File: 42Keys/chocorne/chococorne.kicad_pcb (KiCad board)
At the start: 2 copper layers, 129.4 x 90.4 mm, 54 parts, among them J1 MJ-4PP-9, J2 OLED, SW1 SW_PUSH, SW10 SW_PUSH, SW11 SW_PUSH, SW12 SW_PUSH, SW13 SW_PUSH, SW14 SW_PUSH, SW15 SW_PUSH, SW16 SW_PUSH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

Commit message: But, is it a corne?
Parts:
- moved SW19 1.75 mm to (133.3, 113.8)
- moved SW20 1.75 mm to (153.3, 116.4)
- moved SW21 1.75 mm to (174.6, 119.7)
- moved D21 0.53 mm to (167.4, 92.7)
- moved J2 0.50 mm to (173.7, 90.5)
- moved JP61 0.50 mm to (173.7, 87.9)
- moved JP63 0.50 mm to (176.2, 87.8)
- moved JP64 0.50 mm to (176.2, 87.8)
- moved JP65 0.50 mm to (178.8, 87.8)
- moved JP66 0.50 mm to (178.8, 87.8)
- moved JP68 0.50 mm to (181.4, 87.8)
- moved JP6 0.50 mm to (181.4, 87.8)
- moved JP62 0.50 mm to (173.7, 87.9)
- moved U1 0.44 mm to (178.4, 71.4)
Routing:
- net row0: track 130.1 -> 157.8 mm, vias 1 -> 0
- net Net-(U1-Pad13): track 23.3 -> 38.5 mm, vias 1 -> 0
- net reset: track 59.6 -> 67.3 mm
- net data: track 69.6 -> 77.2 mm
- net Net-(U1-Pad11): track 33.2 -> 26.2 mm
- net SDA: track 64.5 -> 70.5 mm, vias 2 -> 1
- net GND: track 93.8 -> 88.4 mm, vias 0 -> 1
- net Net-(U1-Pad24): track 46.0 -> 50.5 mm
- net Net-(U1-Pad14): track 29.9 -> 26.1 mm
- net VCC: track 61.6 -> 57.8 mm, vias 0 -> 1
- net col1: track 188.0 -> 191.5 mm
- net Net-(D19-Pad2): track 30.6 -> 27.4 mm
- net Net-(D21-Pad2): track 33.4 -> 31.2 mm
- net LED: track 17.1 -> 18.9 mm
- net col5: track 84.2 -> 82.6 mm, vias 1 -> 0
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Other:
- board size 129.4 x 90.4 mm -> 130 x 88.6 mm

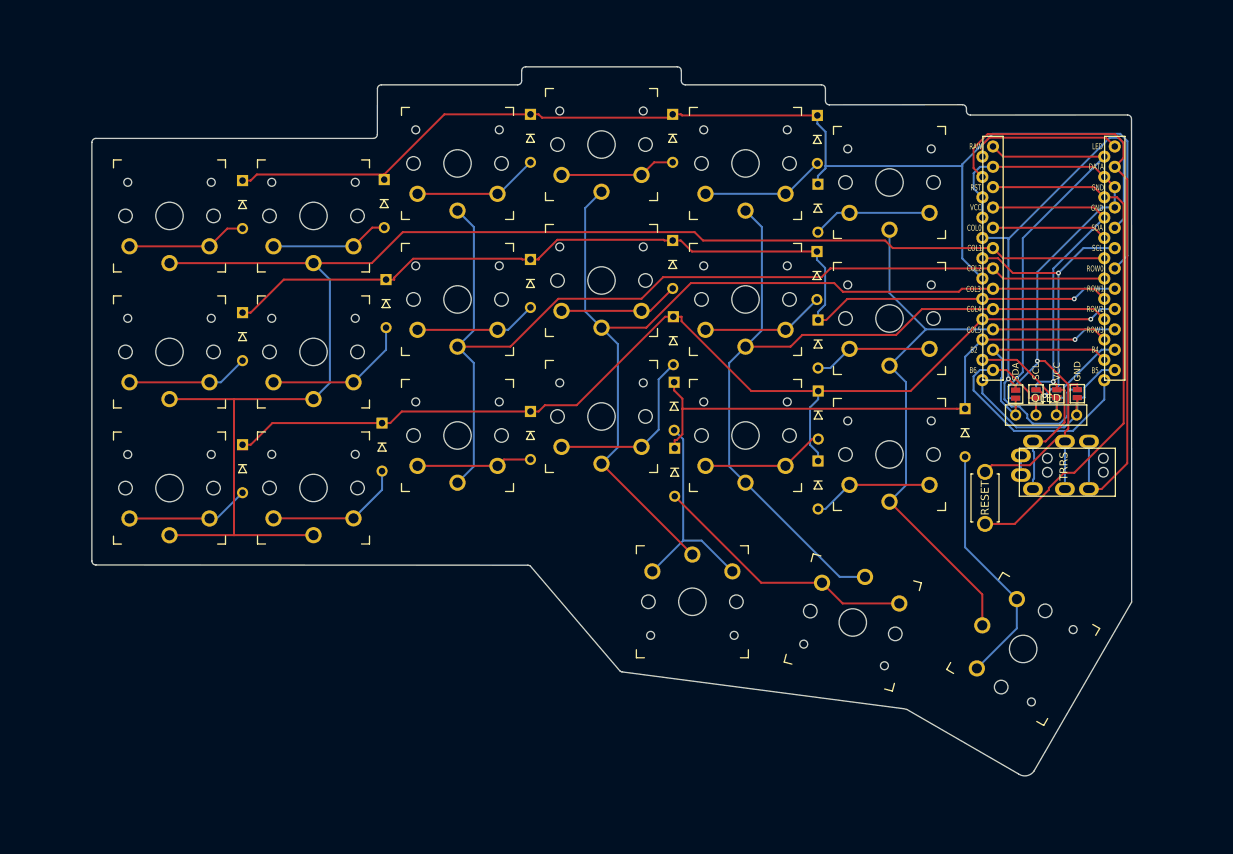
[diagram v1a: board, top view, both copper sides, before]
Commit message: Add back break off, 'fix' 1.5u footprint (maybe) move bits around.
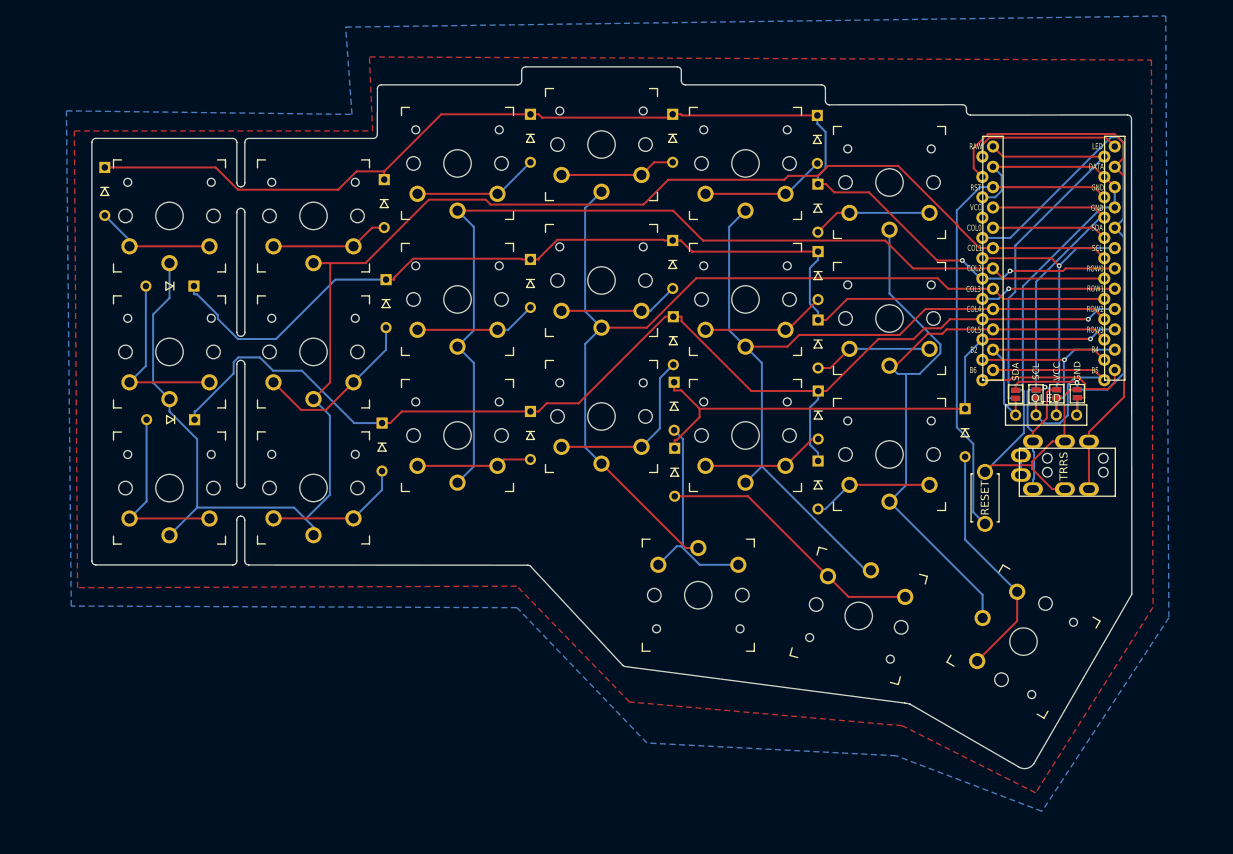
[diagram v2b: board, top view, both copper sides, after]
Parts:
- moved D1 17.3 mm to (59.8, 62.5)
- moved D7 11.1 mm to (68.0, 74.3), turned to 180 degrees
- moved D13 10.9 mm to (68.0, 91.0), turned to 180 degrees
- moved SW20 1.10 mm to (154.1, 115.6)
- moved SW19 1.10 mm to (134.0, 113.0)
- moved SW21 0.92 mm to (174.7, 118.8)
- moved D11 0.14 mm to (149.0, 73.0)
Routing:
- net row2: track 133.7 -> 146.6 mm
- net row1: track 124.5 -> 135.8 mm
- net row0: track 157.8 -> 148.0 mm, vias 0 -> 2
- net col5: track 82.6 -> 91.4 mm
- net col1: track 191.5 -> 199.3 mm
- net Net-(D13-Pad2): track 15.5 -> 23.2 mm
- net Net-(D7-Pad2): track 15.3 -> 22.9 mm
- net data: track 77.2 -> 70.0 mm
- net reset: track 67.3 -> 60.8 mm
- net Net-(U1-Pad13): track 38.5 -> 32.4 mm
- net GND: track 88.4 -> 94.4 mm, vias 1 -> 0
- net VCC: track 57.8 -> 61.8 mm, vias 1 -> 0
- net Net-(D8-Pad2): track 18.5 -> 21.4 mm
- net SDA: track 70.5 -> 68.9 mm
- net Net-(U1-Pad12): track 27.1 -> 26.0 mm
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- added copper zone on B.Cu, net (none)
- added copper zone on F.Cu, net (none)
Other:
- board size 130 x 88.6 mm -> 130 x 87.7 mm

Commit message: tweaks
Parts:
- added H1: h1, kbd:LEGO_HOLE, F.Cu at (185.7, 106.1)
- added h2: h2, kbd:LEGO_HOLE, F.Cu at (171.2, 97.6)
- D1, D10, D11, D12, D13, D14, D15, D16, D17, D18, D19, D2, D20, D21, D3, D4, D5, D6, D7, D8, D9: footprint kbd:D3_TH -> kbd:D3_TH_SMD
- moved RSW1 19.0 mm to (186.0, 90.9)
- moved D21 18.8 mm to (149.1, 97.1)
- moved D18 12.0 mm to (149.1, 87.2)
- moved D19 9.62 mm to (139.3, 84.5), turned to 0 degrees
- moved D17 9.17 mm to (157.4, 86.9), turned to 0 degrees
- moved D11 8.68 mm to (157.1, 69.9), turned to 0 degrees
- moved D12 4.92 mm to (148.9, 76.7)
- moved D20 3.55 mm to (130.9, 94.1)
- moved D10 3.29 mm to (130.9, 68.4)
- moved J1 3.13 mm to (188.0, 100.2)
- moved D6 1.78 mm to (148.9, 66.4)
- moved J2 1.06 mm to (173.9, 89.4)
- moved JP6 1.06 mm to (181.6, 86.8)
- moved JP61 1.06 mm to (173.9, 86.8)
- moved JP62 1.06 mm to (173.9, 86.8)
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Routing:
- net row0: track 148.0 -> 168.3 mm, vias 2 -> 0
- net SDA: track 68.9 -> 49.9 mm, vias 1 -> 2
- net row1: track 135.8 -> 153.9 mm, vias 1 -> 0
- net Net-(D17-Pad2): track 15.5 -> 33.0 mm
- net Net-(D11-Pad2): track 15.6 -> 32.6 mm
- net Net-(D19-Pad2): track 27.0 -> 40.5 mm
- net reset: track 60.8 -> 48.4 mm
- net row2: track 146.6 -> 158.5 mm
- net Net-(D21-Pad2): track 30.3 -> 42.1 mm
- net GND: track 94.4 -> 83.3 mm, vias 0 -> 1
- net Net-(U1-Pad13): track 32.4 -> 23.5 mm
- net Net-(D18-Pad2): track 15.2 -> 23.8 mm
- net VCC: track 61.8 -> 69.9 mm, vias 0 -> 2
- net row3: track 71.3 -> 78.8 mm
- net Net-(D10-Pad2): track 15.1 -> 21.0 mm
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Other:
- outline, holes or cut-outs redrawn

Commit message: fix screens?
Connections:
- U1 pad 11: Net-(U1-Pad11) -> (no net)
- U1 pad 12: Net-(U1-Pad12) -> (no net)
- U1 pad 13: Net-(U1-Pad13) -> (no net)
- U1 pad 14: Net-(U1-Pad14) -> (no net)
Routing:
- net Net-(U1-Pad14): track 25.4 -> 2.11 mm
- net Net-(U1-Pad11): track 27.3 -> 4.36 mm, vias 1 -> 0
- net Net-(U1-Pad12): track 26.0 -> 4.42 mm
- net col5: track 89.0 -> 109.7 mm
- net Net-(U1-Pad13): track 23.5 -> 4.27 mm
- net data: track 72.0 -> 62.0 mm
- net col3: track 121.7 -> 129.3 mm, vias 1 -> 0
- net Net-(U1-Pad24): track 46.0 -> 52.7 mm
- net VCC: track 69.9 -> 76.5 mm, vias 2 -> 1
- net GND: track 83.3 -> 89.8 mm, vias 1 -> 0
- net col2: track 125.1 -> 129.0 mm, vias 1 -> 0
- net col1: track 196.7 -> 199.3 mm
- net Net-(D21-Pad2): track 42.1 -> 44.4 mm
- net SDA: track 49.9 -> 52.2 mm, vias 2 -> 1
- net col4: track 105.3 -> 107.3 mm
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
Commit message: really fix screen, try not to route vcc to gnd...
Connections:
- JP62 pad 2: Net-(U1-Pad24) -> Net-(U1-Pad14)
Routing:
- net Net-(U1-Pad24): track 52.7 -> 14.4 mm
- net col5: track 109.7 -> 83.1 mm
- net Net-(D17-Pad2): track 32.9 -> 46.9 mm
- net SDA: track 52.2 -> 44.7 mm, vias 1 -> 2
- net col2: track 129.0 -> 122.8 mm
- net GND: track 89.8 -> 83.8 mm
- net col3: track 129.3 -> 124.6 mm
- net VCC: track 76.5 -> 79.4 mm, vias 1 -> 0
- net row0: track 167.9 -> 170.8 mm, vias 0 -> 1
- net Net-(D21-Pad2): track 44.4 -> 42.1 mm
- net Net-(U1-Pad14): track 2.11 -> 4.21 mm
- net row1: track 152.5 -> 154.6 mm
- net row3: track 80.3 -> 78.4 mm, vias 0 -> 1
- net row2: track 159.7 -> 158.0 mm, vias 0 -> 1
- net col4: track 107.3 -> 106.2 mm
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
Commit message: manual routing.
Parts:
- moved D11 1.00 mm to (158.1, 69.9)
- moved D6 0.50 mm to (148.9, 66.9)
- turned RSW1 to 270 degrees
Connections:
- SW1 pad 1: col1 -> col0
- SW13 pad 1: col1 -> col0
- SW7 pad 1: col1 -> col0
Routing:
- net col0: track 14.4 -> 182.0 mm, vias 0 -> 1
- net col1: track 198.6 -> 153.5 mm, vias 0 -> 1
- net SCL: track 35.8 -> 80.8 mm, vias 2 -> 1
- net SDA: track 44.7 -> 61.7 mm, vias 2 -> 1
- net row2: track 158.0 -> 171.0 mm
- net Net-(D19-Pad2): track 40.5 -> 53.1 mm
- net col2: track 122.8 -> 134.3 mm, vias 0 -> 1
- net Net-(D17-Pad2): track 46.9 -> 35.4 mm
- net col5: track 83.1 -> 94.2 mm, vias 0 -> 1
- net VCC: track 79.4 -> 68.9 mm
- net GND: track 83.8 -> 92.9 mm, vias 0 -> 1
- net row1: track 154.6 -> 163.0 mm
- net row3: track 78.4 -> 85.6 mm
- net col4: track 106.2 -> 113.0 mm, vias 0 -> 1
- net row0: track 170.8 -> 177.1 mm
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
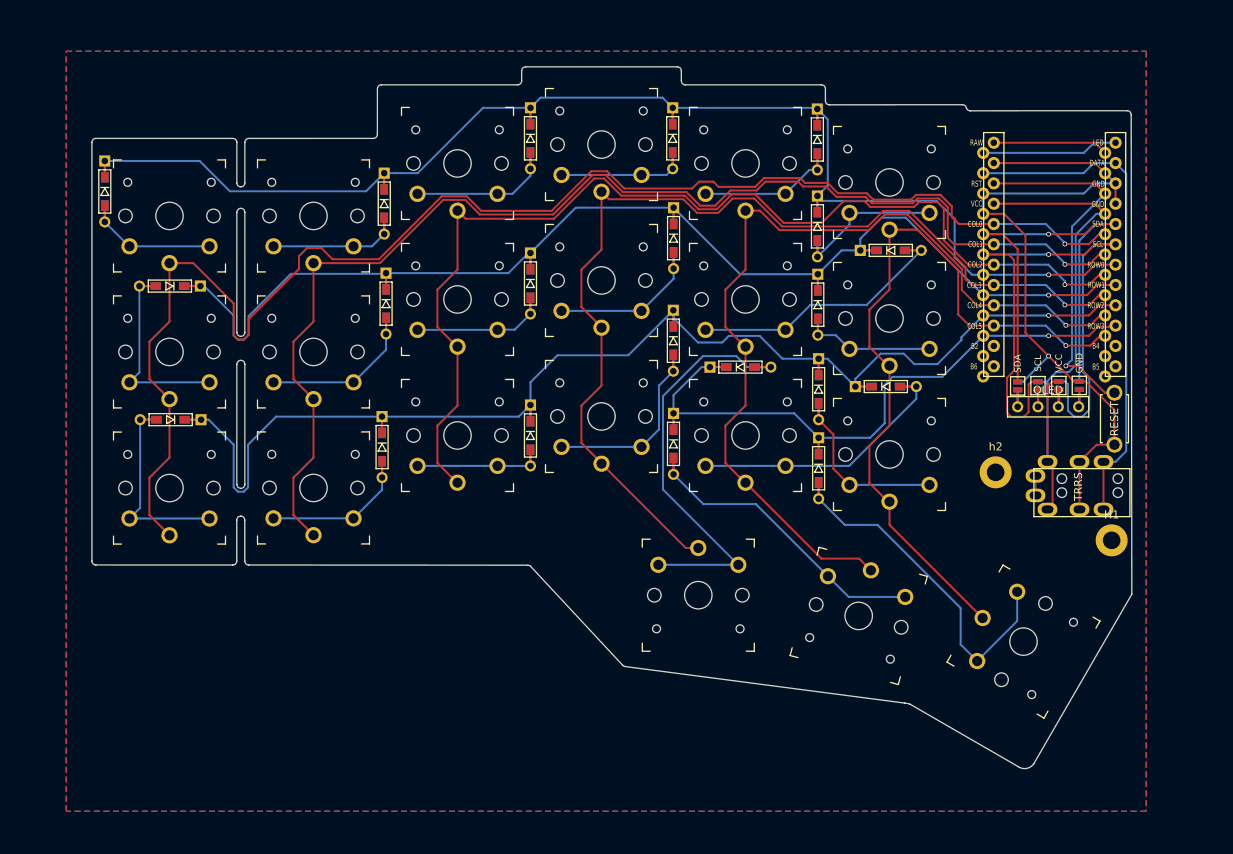
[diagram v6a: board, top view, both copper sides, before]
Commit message: delete somome bits that were really bad or superceded
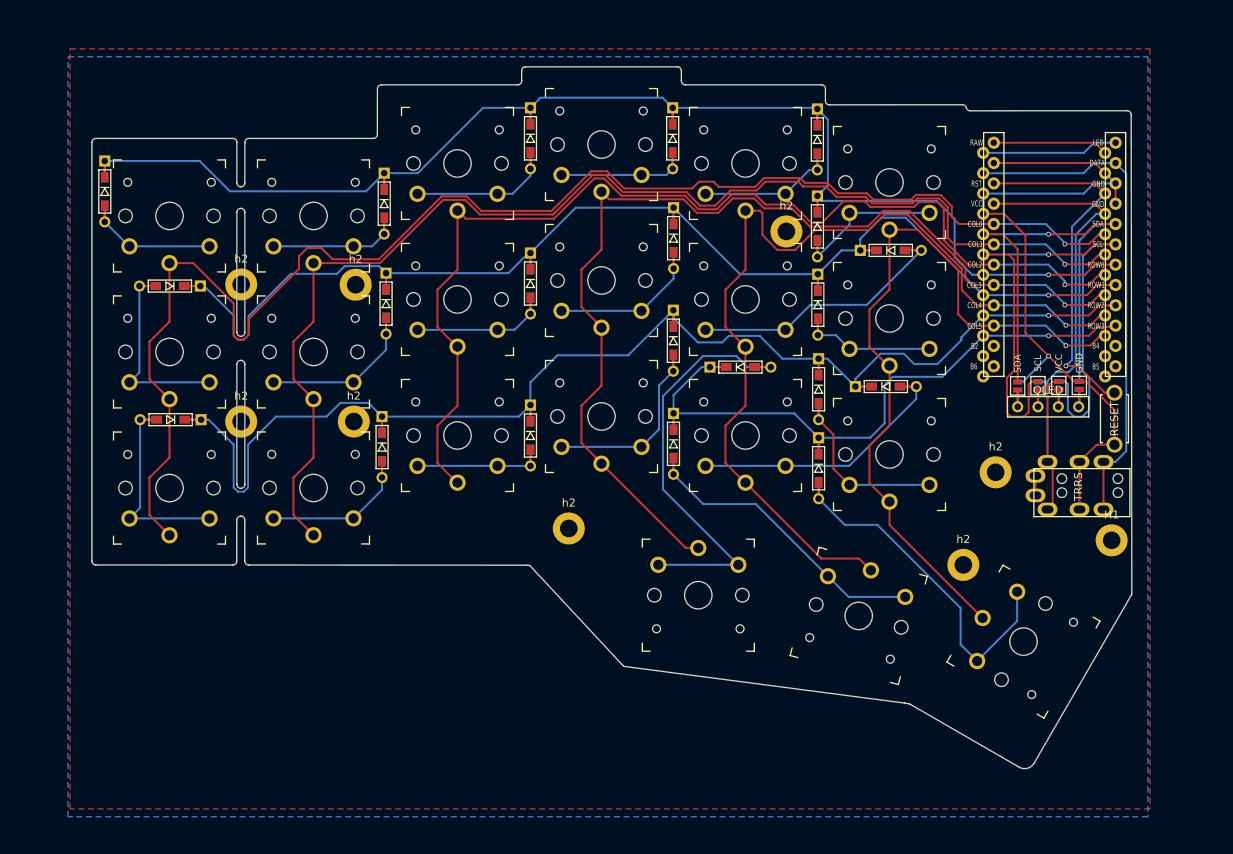
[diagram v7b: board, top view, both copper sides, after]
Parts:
- added h2: h2, kbd:LEGO_HOLE, F.Cu at (91.0, 91.3)
- added h2: h2, kbd:LEGO_HOLE, F.Cu at (76.9, 91.3)
- added h2: h2, kbd:LEGO_HOLE, F.Cu at (167.1, 109.2)
- added h2: h2, kbd:LEGO_HOLE, F.Cu at (117.8, 104.7)
- added h2: h2, kbd:LEGO_HOLE, F.Cu at (76.9, 74.2)
- added h2: h2, kbd:LEGO_HOLE, F.Cu at (145.0, 67.5)
- added h2: h2, kbd:LEGO_HOLE, F.Cu at (91.2, 74.2)
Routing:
- net col4: track 113.0 -> 116.6 mm
- net row2: track 171.0 -> 172.4 mm
- net row1: track 163.0 -> 163.7 mm
